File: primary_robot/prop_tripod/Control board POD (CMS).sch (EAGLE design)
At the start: 94 parts, among them IC3 NE555D, Q1 MOSFET-NCHANNELD2PAK, Q2 MOSFET-NCHANNELD2PAK, Q3 MOSFET-NCHANNELD2PAK, Q4 MOSFET-NCHANNELD2PAK

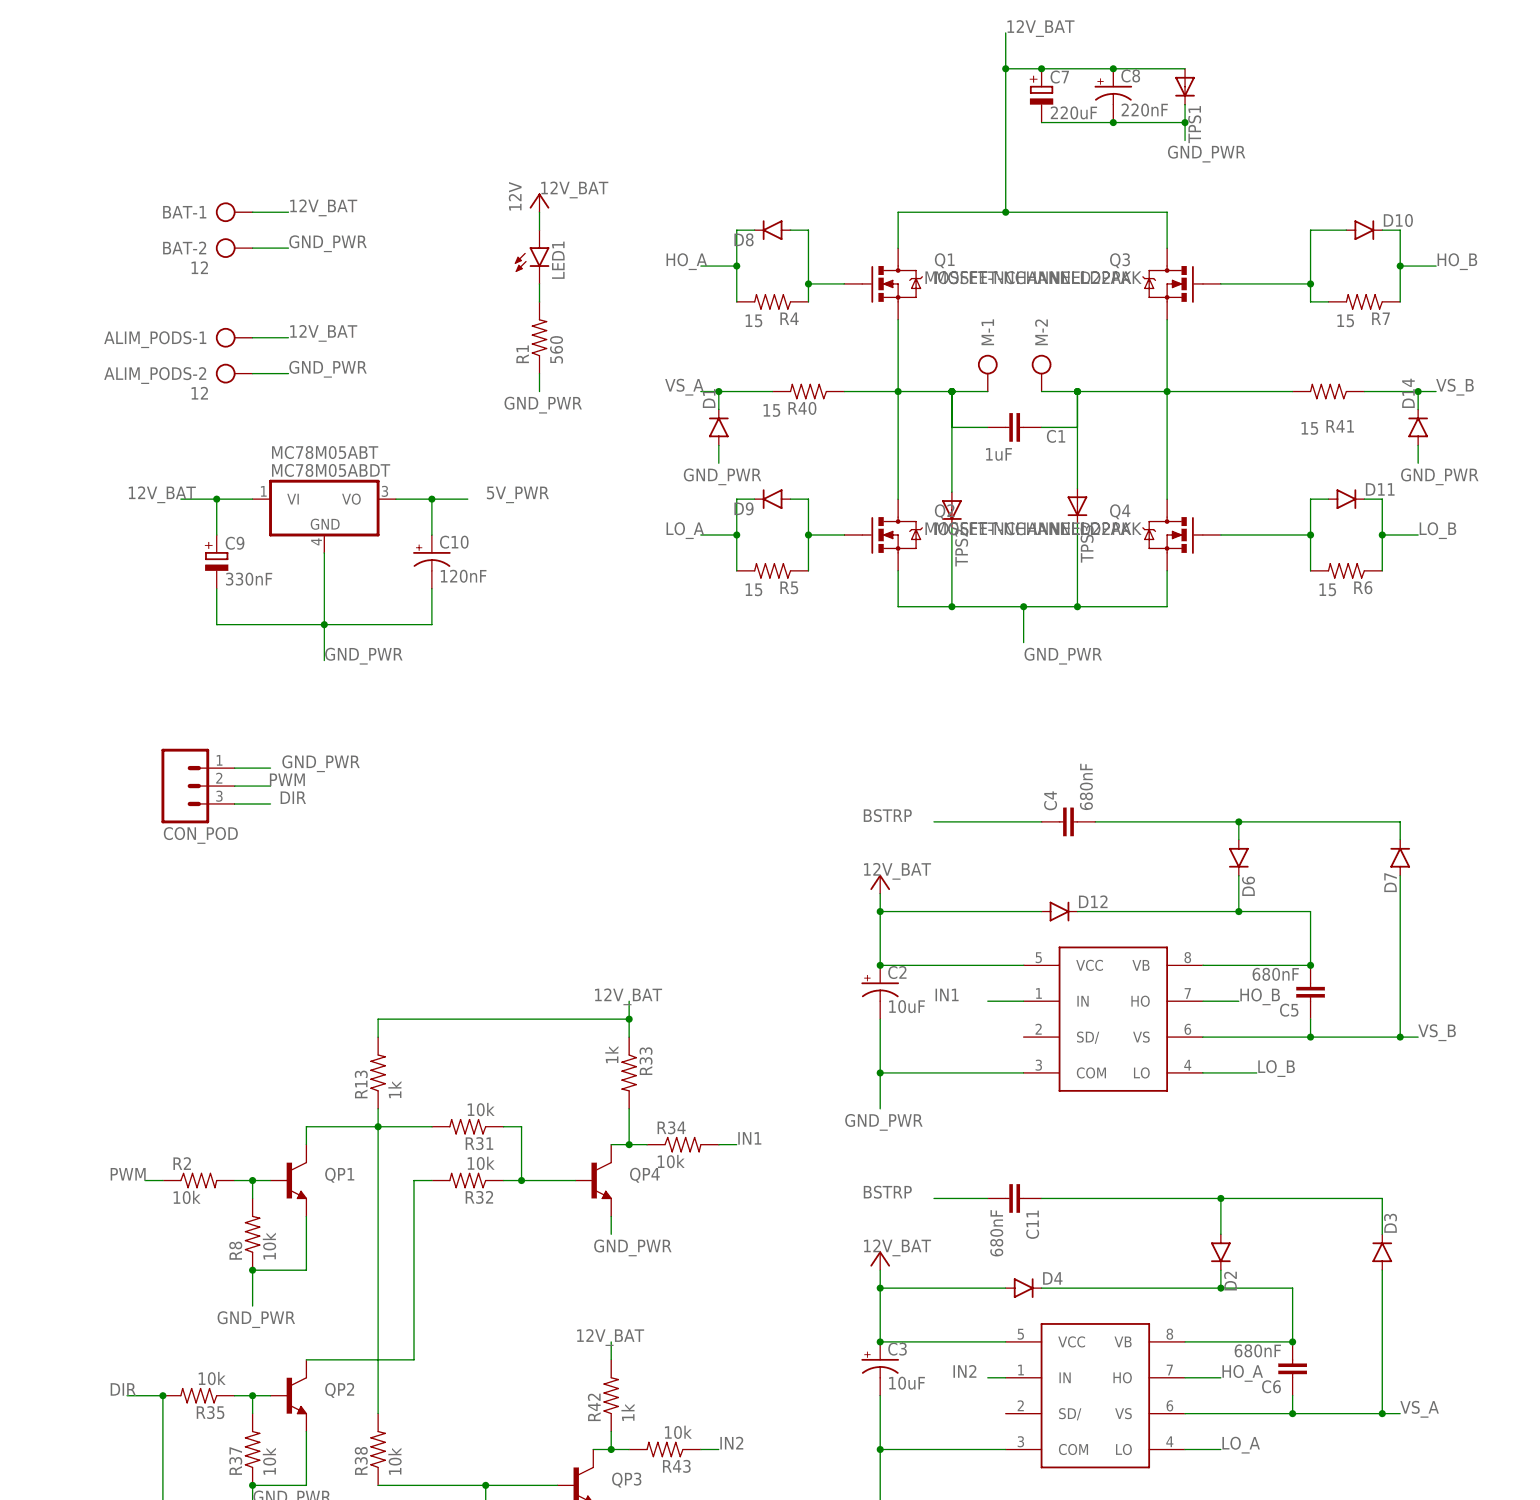
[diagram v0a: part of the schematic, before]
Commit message: [prop_tripod] Updates to pre-Rev2
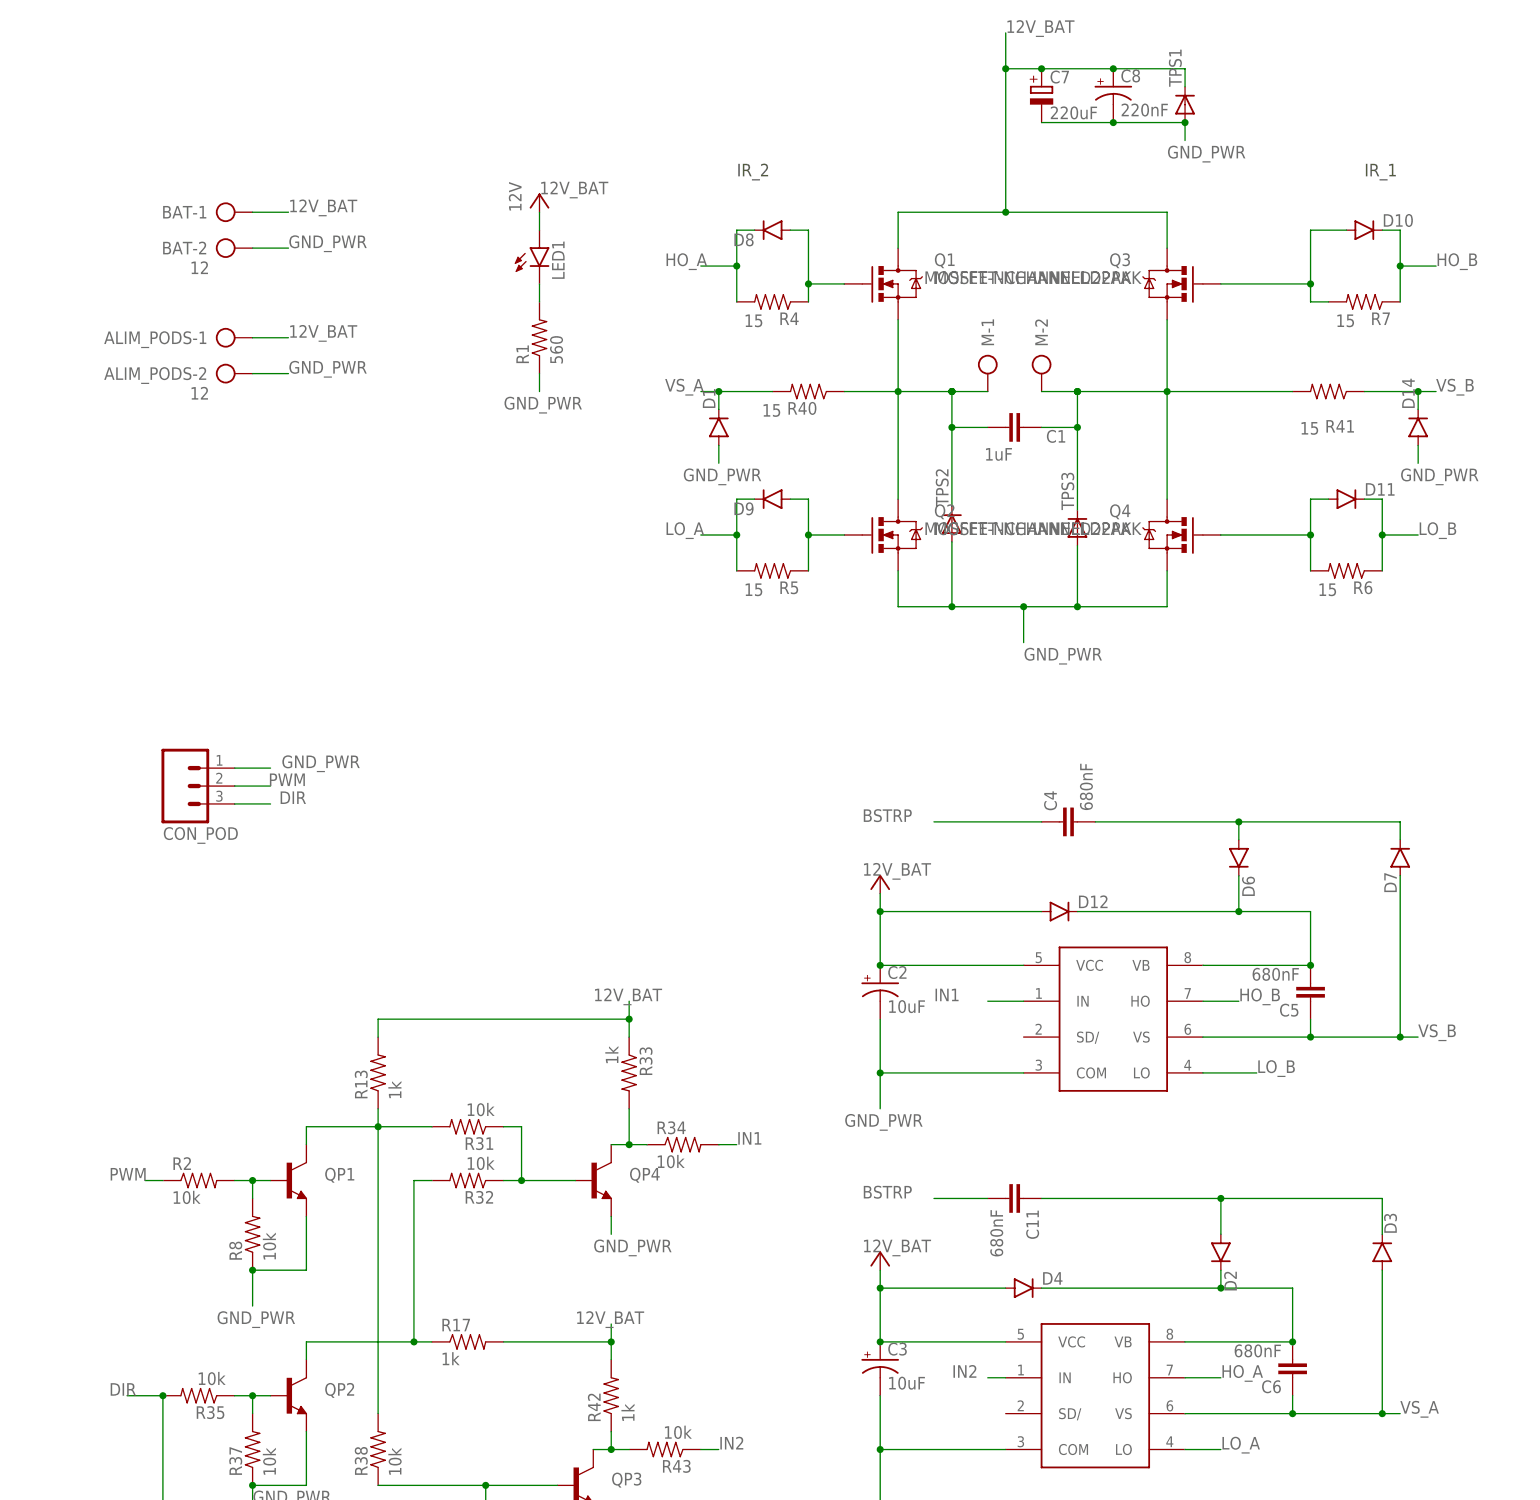
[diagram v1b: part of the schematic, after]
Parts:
- removed C10: 120nF, resistor:CPOL-USA/3216-18W
- removed C9: 330nF, rcl:CPOL-EUA/3216-18R
- removed MC78M05ABT: MC78M05ABDT, linear:MC78M05ABDT
- added R17: 1k, SparkFun-Passives:RESISTOR0603-RES
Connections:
- removed net 5V_PWR: C10.+, MC78M05ABT.VO
- net 12V_BAT: now also R17.2, TPS1.C; no longer C9.+, MC78M05ABT.VI, TPS1.A
- net GND_PWR: now also TPS1.A, TPS2.A, TPS3.A; no longer C10.-, C9.-, MC78M05ABT.GND, TPS1.C, TPS2.C, TPS3.C
- net N$11: now also TPS2.C; no longer TPS2.A
- net N$3: now also TPS3.C; no longer TPS3.A
- net N$64: now also R17.1
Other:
- note added: "IR_1"
- note added: "IR_2"
- moved on the sheet: TPS1, TPS2, TPS3

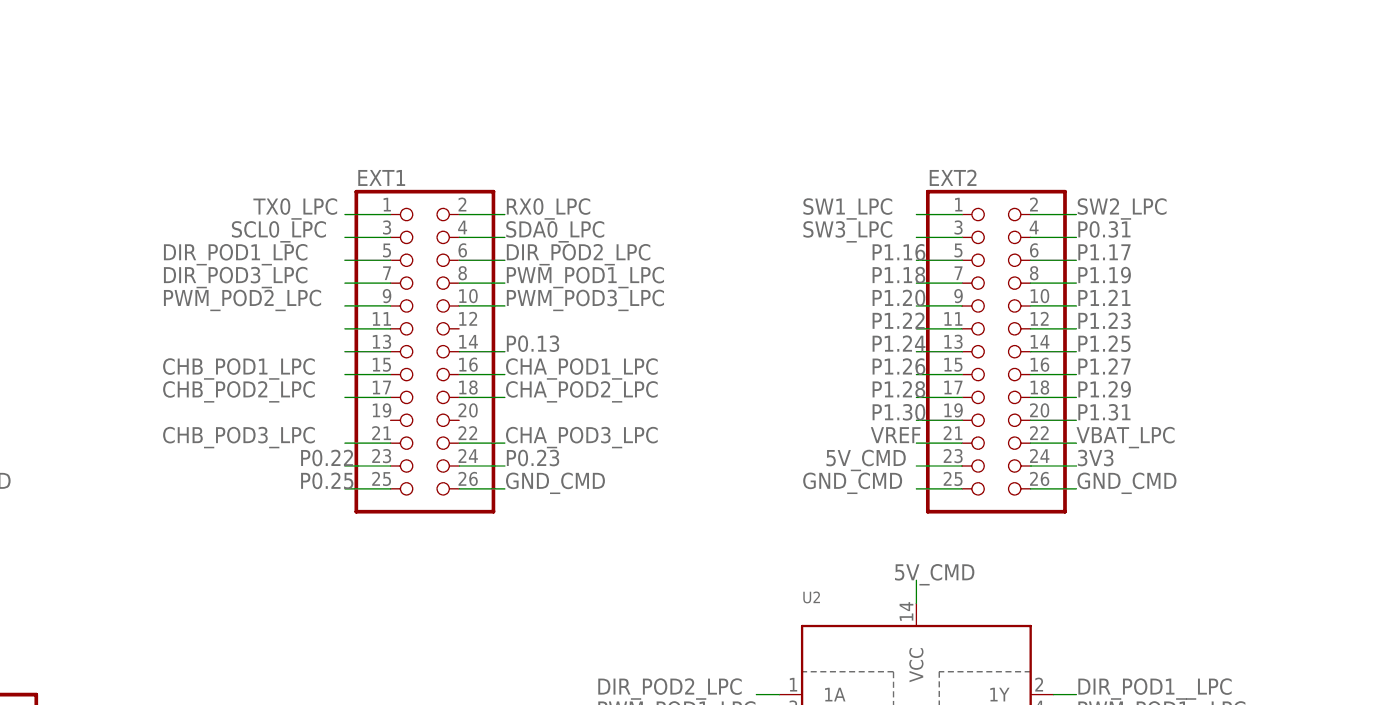
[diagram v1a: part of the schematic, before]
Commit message: [prop_tripod] Fixes RST connection
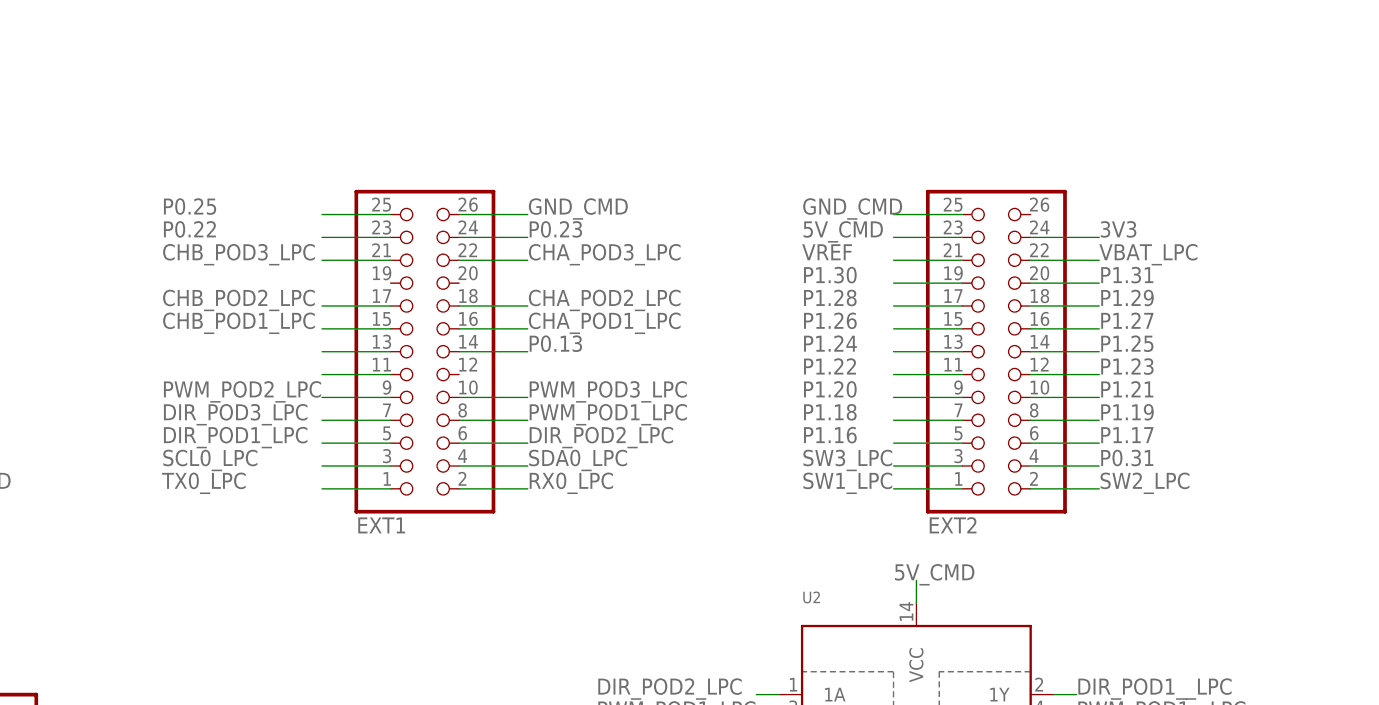
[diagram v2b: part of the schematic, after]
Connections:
- net GND_CMD: no longer EXT2.26
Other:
- moved on the sheet: EXT1, EXT2

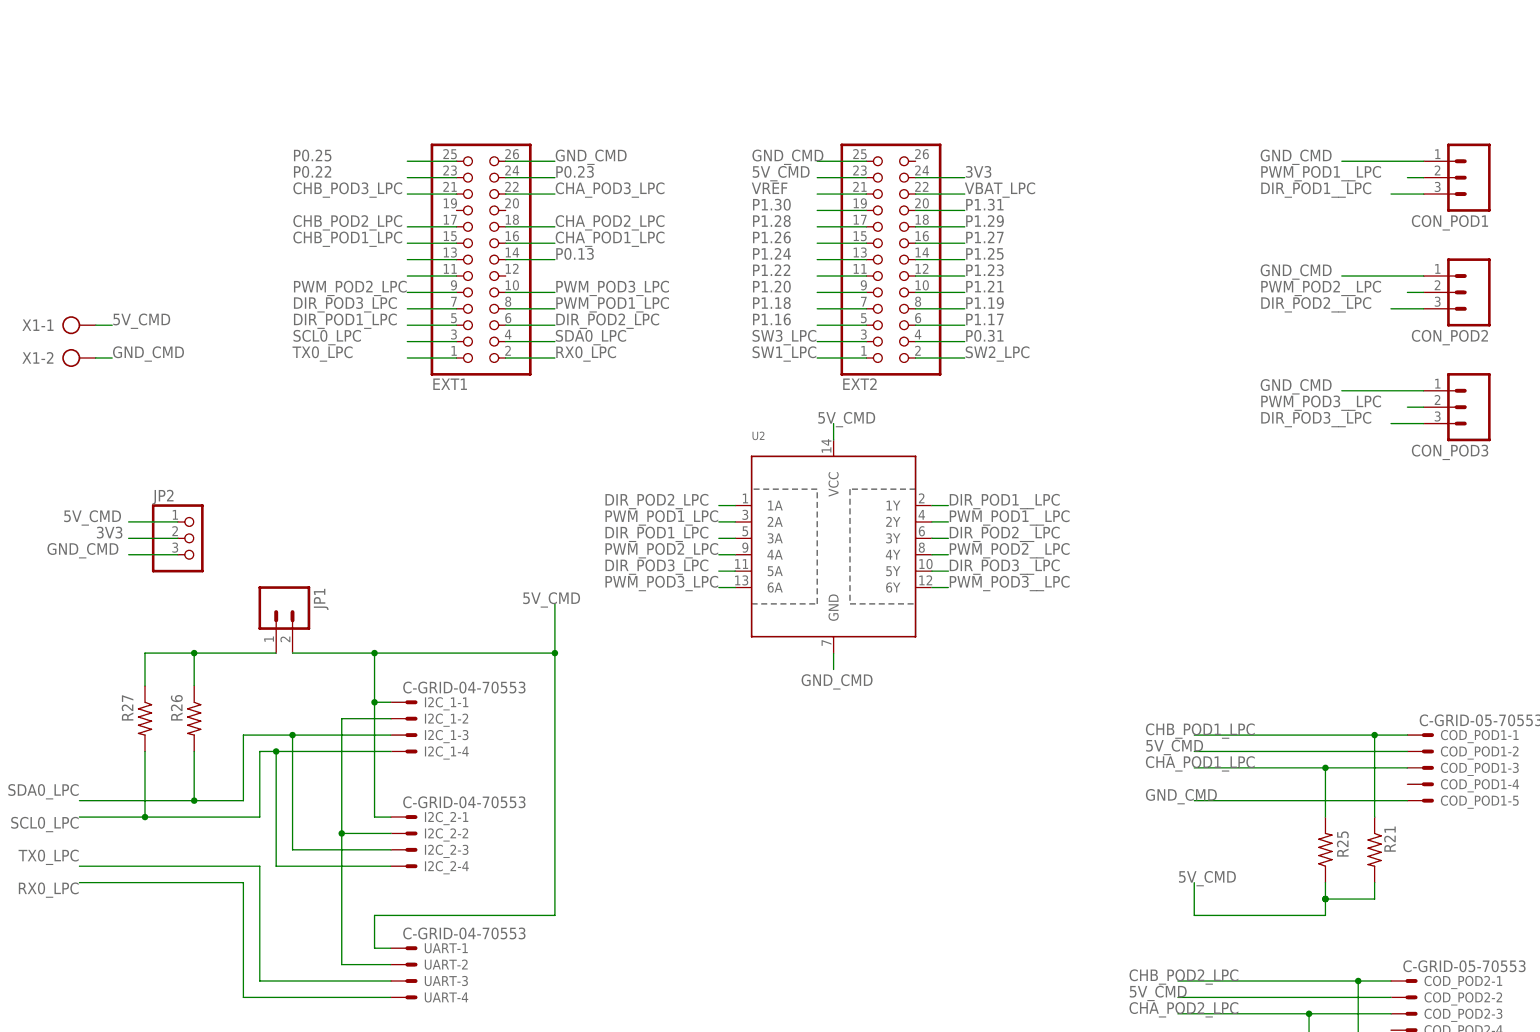
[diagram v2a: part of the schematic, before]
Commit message: [prop_tripod] Fixes buffer pull-ups + I²C pull-ups headers
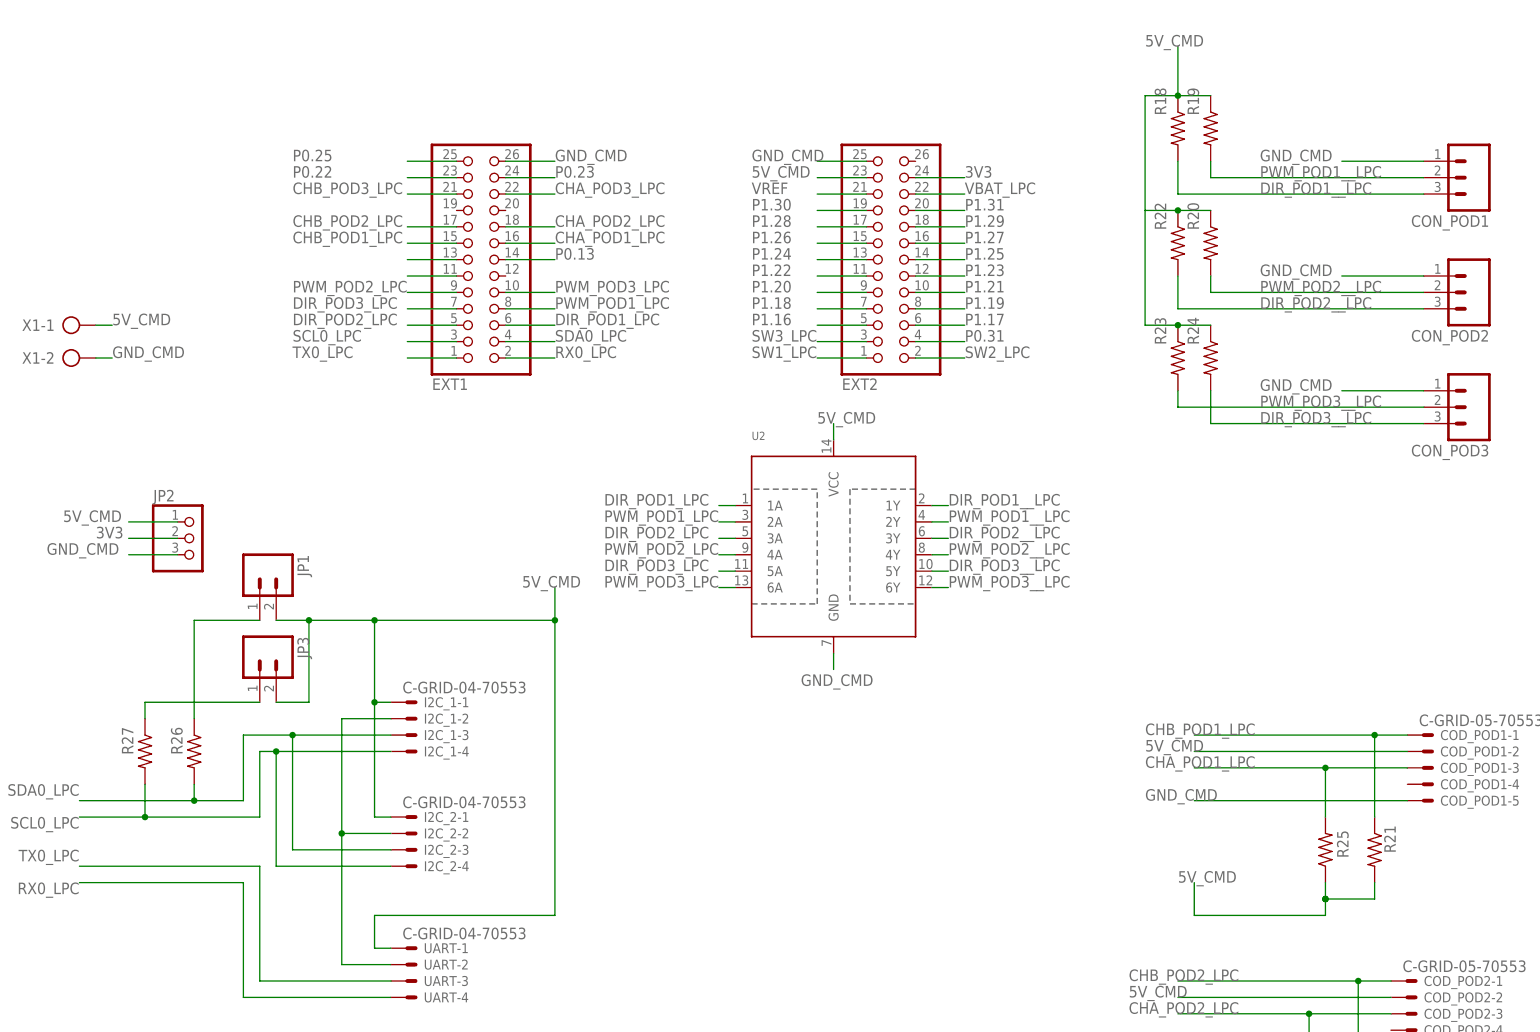
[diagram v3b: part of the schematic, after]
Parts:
- added JP3: (no value), SparkFun:M02PTH
- added R18, R19, R20, R22, R23, R24: 3.3k, SparkFun-Passives:RESISTOR0603-RES
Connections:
- new net N$54: JP3.1, R27.1
- net 5V_CMD: now also JP3.2, R18.1, R19.1, R20.1, R22.1, R23.1, R24.1
- net DIR_POD1_LPC: now also EXT1.6, U2.1A; no longer EXT1.5, U2.3A
- net DIR_POD1__LPC: now also R18.2
- net DIR_POD2_LPC: now also EXT1.5, U2.3A; no longer EXT1.6, U2.1A
- net DIR_POD2__LPC: now also R22.2
- net DIR_POD3__LPC: now also R24.2
- net N$52: no longer R27.1
- net PWM_POD1__LPC: now also R19.2
- net PWM_POD2__LPC: now also R20.2
- net PWM_POD3__LPC: now also R23.2
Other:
- moved on the sheet: JP1, R26, R27
